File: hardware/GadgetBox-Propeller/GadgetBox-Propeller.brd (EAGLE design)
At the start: 93.5 x 53.5 mm, 13 parts, among them IC1 P8X32A-Q44

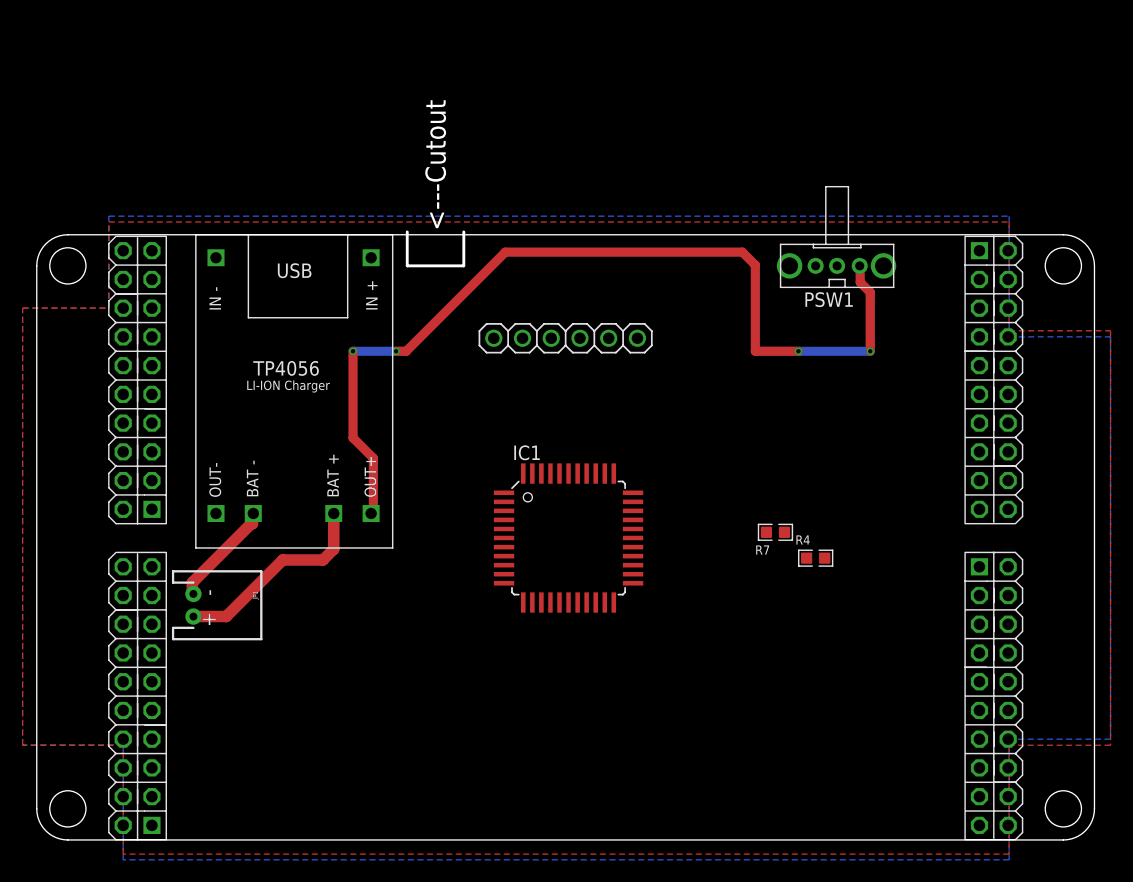
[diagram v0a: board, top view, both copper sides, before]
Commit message: mostly done routing
added EEPROM and most routing
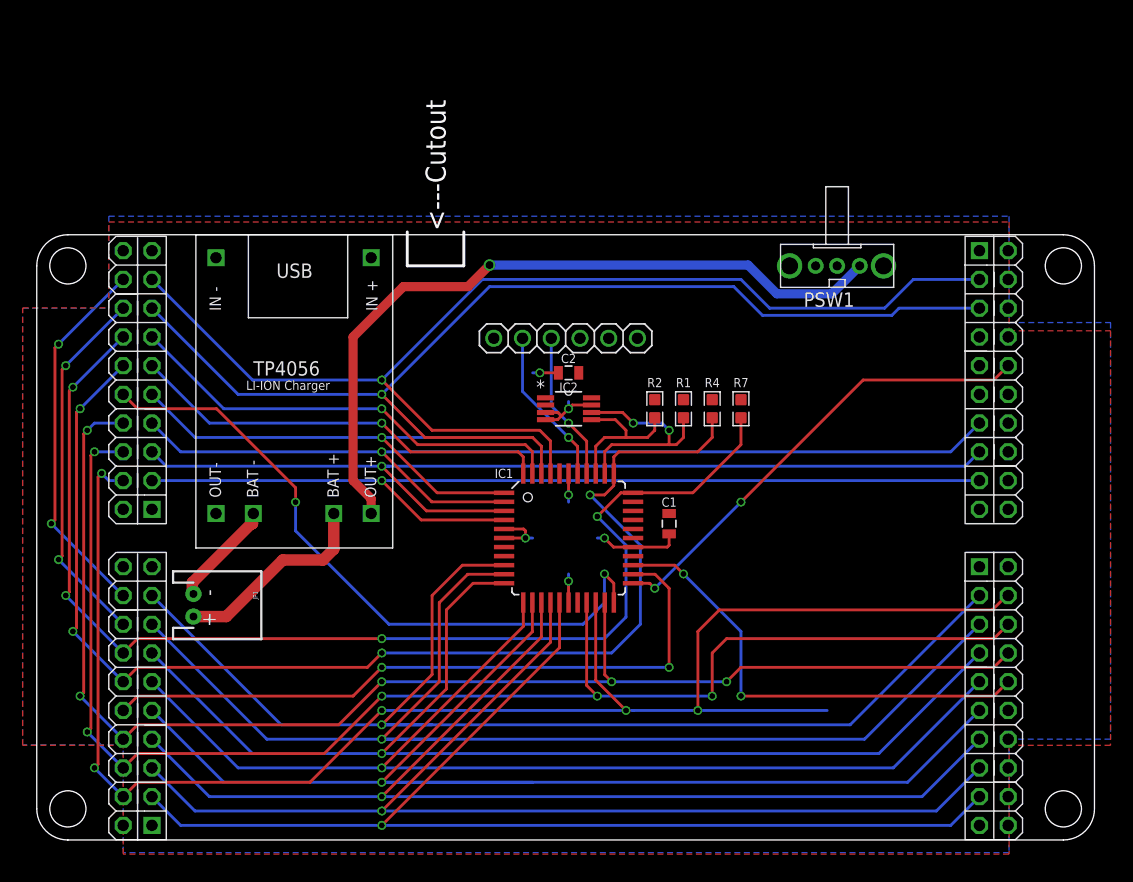
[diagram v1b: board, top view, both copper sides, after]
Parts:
- added C1, C2: (no value), SparkFun-Passives:0805
- added IC2: 24LC256-I/MS, Microchip_By_element14_Batch_1:SOP65P490X110-8N
- added R1, R2: 10K, GadgetFactory:0603
- moved R4 16.1 mm to (61.0, 39.4), turned to 90 degrees
- moved R7 11.3 mm to (63.5, 39.4), turned to 90 degrees
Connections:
- net 3V3: now also C1.1, C2.1, IC2.8, R1.2, R2.2
- net EEPROM-SCL: now also IC2.6, R1.1
- net EEPROM-SDA: now also IC2.5, R2.1
- net GND: now also C1.2, C2.2, IC2.3, IC2.4, IC2.7
- net IO0: now also AL.G0
- net IO1: now also AL.G1
- net IO2: now also AL.G2
- net IO3: now also AL.G3
- net IO4: now also AL.G4
- net IO5: now also AL.G5
- net IO6: now also AL.G6
- net IO7: now also AL.G7
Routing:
- net SPI-MISO: track 0.00 -> 143.8 mm, vias 0 -> 5
- net SPI-MOSI: track 0.00 -> 126.4 mm, vias 0 -> 5
- net SPI-SCK: track 0.00 -> 121.2 mm, vias 0 -> 5
- net IO12: track 0.00 -> 113.2 mm, vias 0 -> 1
- net IO9: track 0.00 -> 108.9 mm, vias 0 -> 1
- net I2C-SDA: track 0.00 -> 108.8 mm, vias 0 -> 4
- net IO8: track 0.00 -> 107.8 mm, vias 0 -> 1
- net I2C-SCL: track 0.00 -> 105.6 mm, vias 0 -> 4
- net IO0: track 0.00 -> 102.6 mm, vias 0 -> 1
- net IO10: track 0.00 -> 101.7 mm, vias 0 -> 1
- net IO15: track 0.00 -> 101.5 mm, vias 0 -> 1
- net IO14: track 0.00 -> 100.9 mm, vias 0 -> 1
- net IO13: track 0.00 -> 100.4 mm, vias 0 -> 1
- net IO1: track 0.00 -> 100.0 mm, vias 0 -> 1
- net IO11: track 0.00 -> 99.3 mm, vias 0 -> 1
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
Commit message: Propeller mostly done
Need to validate FTDI connection and do eCog graphics
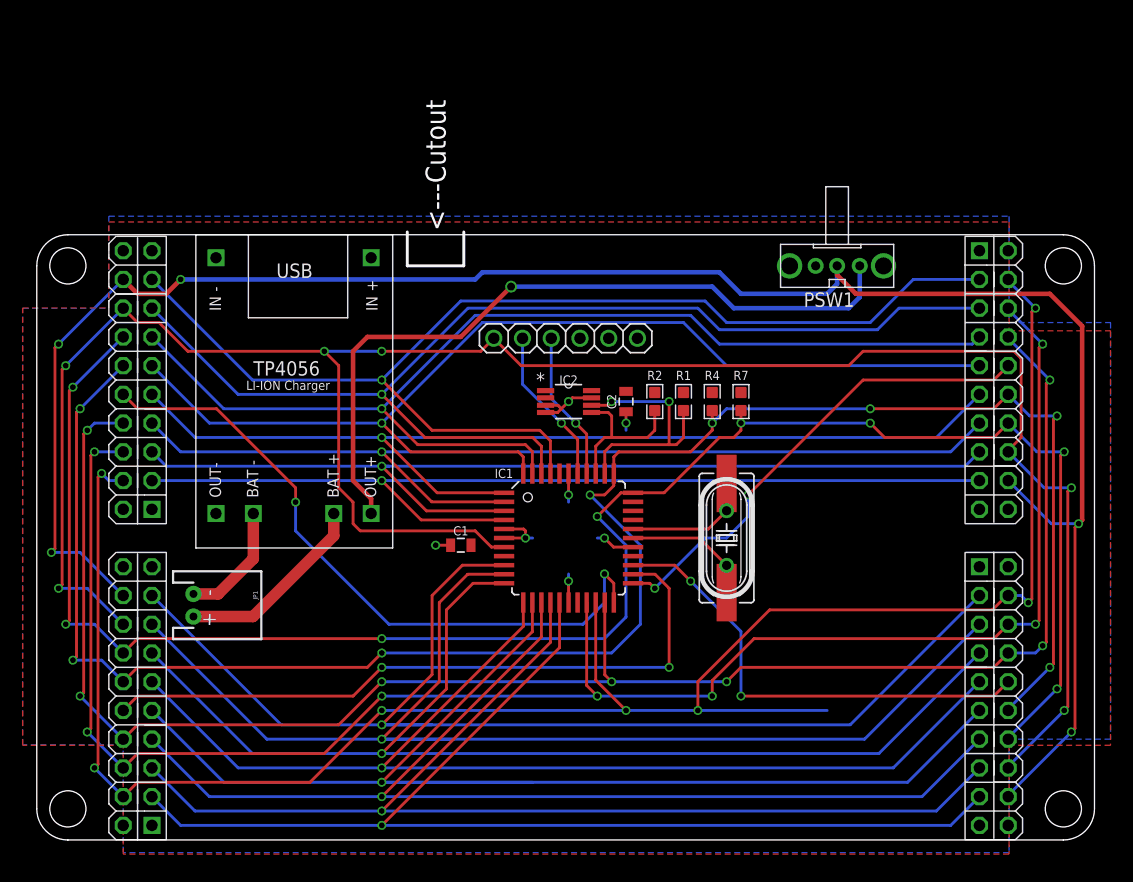
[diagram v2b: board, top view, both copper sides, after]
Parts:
- added Q1: (no value), adafruit:SM49
- added Q3: (no value), adafruit:HC49U-V
- moved C1 18.5 mm to (38.7, 27.3), turned to 180 degrees
- moved C2 5.68 mm to (53.3, 40.0), turned to 270 degrees
- moved IC2 0.64 mm to (48.3, 40.0)
- moved R1 0.64 mm to (58.4, 40.0)
- moved R2 0.64 mm to (55.9, 40.0)
- moved R4 0.64 mm to (61.0, 40.0)
- moved R7 0.64 mm to (63.5, 40.0)
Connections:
- removed net DTR: FTDI.1
- removed net N$1: IC1.7
- new net N$2: IC1.28, Q1.1, Q3.1
- new net N$3: IC1.29, Q1.2, Q3.2
- net RESET: now also FTDI.1, IC1.7
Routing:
- net RESET: track 32.7 -> 190.6 mm, vias 2 -> 6
- net VIN: track 33.2 -> 178.3 mm, vias 2 -> 5
- net I2C-SDA: track 108.8 -> 170.7 mm, vias 4 -> 8
- net I2C-SCL: track 105.6 -> 165.1 mm, vias 4 -> 8
- net IO3: track 37.6 -> 95.7 mm
- net IO2: track 39.8 -> 97.3 mm
- net IO4: track 48.1 -> 89.1 mm
- net SPI-SCK: track 121.2 -> 153.6 mm, vias 5 -> 7
- net SPI-MOSI: track 126.4 -> 156.9 mm, vias 5 -> 7
- net SPI-MISO: track 143.8 -> 173.1 mm, vias 5 -> 7
- net N$2: track 0.00 -> 11.7 mm
- net N$3: track 0.00 -> 11.6 mm
- net GND: track 36.4 -> 33.6 mm, vias 6 -> 7
- net EEPROM-SCL: track 19.9 -> 22.6 mm
- net SPI-CSB: track 41.5 -> 42.6 mm
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
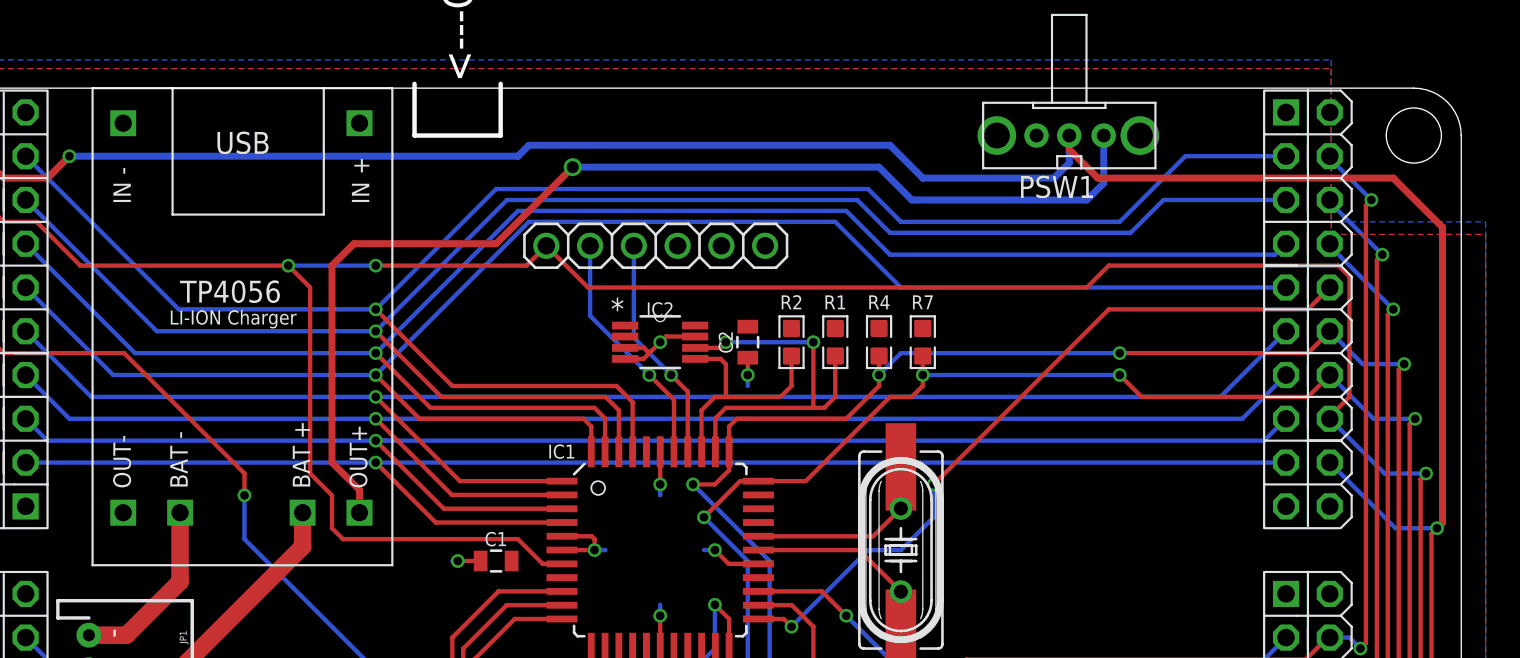
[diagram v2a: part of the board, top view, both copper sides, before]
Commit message: Increased the size of the pads on the battery charge unit to allow surface mount soldering.
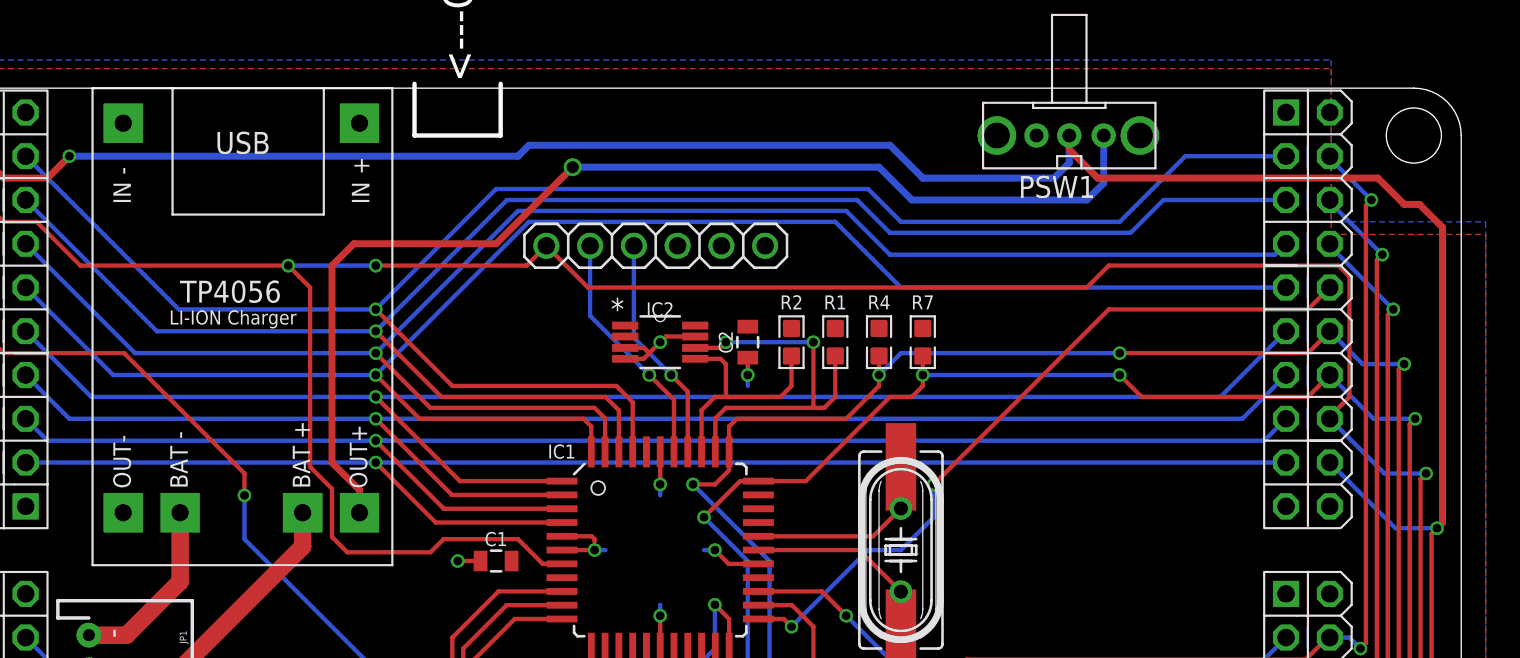
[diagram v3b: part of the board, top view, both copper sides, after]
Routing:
- net RESET: track 190.6 -> 191.5 mm
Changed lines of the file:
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@@
 <setting verticaltext="up"/>
 </settings>
-<grid distance="0.0125" unitdist="inch" unit="inch" style="lines" multiple="1" display="yes" altdistance="0.005" altunitdist="inch" altunit="inch"/>
+<grid distance="0.05" unitdist="inch" unit="inch" style="lines" multiple="1" display="yes" altdistance="0.005" altunitdist="inch" altunit="inch"/>
 <layers>
 <layer number="1" name="Top" color="4" fill="1" visible="yes" active="yes"/>
@@
 <wire x1="42.56" y1="27.14" x2="41.44" y2="27.14" width="0.254" layer="1"/>
 <wire x1="41.44" y1="27.14" x2="40.005" y2="28.575" width="0.254" layer="1"/>
-<wire x1="40.005" y1="28.575" x2="29.845" y2="28.575" width="0.254" layer="1"/>
-<wire x1="29.845" y1="28.575" x2="29.21" y2="29.21" width="0.254" layer="1"/>
-<wire x1="29.21" y1="29.21" x2="29.21" y2="31.115" width="0.254" layer="1"/>
-<wire x1="29.21" y1="31.115" x2="27.94" y2="32.385" width="0.254" layer="1"/>
-<wire x1="27.94" y1="32.385" x2="27.94" y2="43.18" width="0.254" layer="1"/>
+<wire x1="27.94" y1="34.925" x2="27.94" y2="35.433" width="0.254" layer="1"/>
+<wire x1="27.94" y1="35.433" x2="27.94" y2="43.18" width="0.254" layer="1"/>
 <wire x1="27.94" y1="43.18" x2="26.67" y2="44.45" width="0.254" layer="1"/>
 <via x="26.67" y="44.45" extent="1-16" drill="0.5"/>
@@
 <wire x1="73.025" y1="43.18" x2="44.07" y2="43.18" width="0.254" layer="1"/>
 <wire x1="44.07" y1="43.18" x2="41.65" y2="45.6" width="0.254" layer="1"/>
+<wire x1="40.005" y1="28.575" x2="35.687" y2="28.575" width="0.254" layer="1"/>
+<wire x1="35.687" y1="28.575" x2="34.925" y2="27.813" width="0.254" layer="1"/>
+<wire x1="34.925" y1="27.813" x2="30.099" y2="27.813" width="0.254" layer="1"/>
+<wire x1="30.099" y1="27.813" x2="29.21" y2="28.702" width="0.254" layer="1"/>
+<wire x1="29.21" y1="28.702" x2="29.21" y2="31.496" width="0.254" layer="1"/>
+<wire x1="29.21" y1="31.496" x2="27.94" y2="32.766" width="0.254" layer="1"/>
+<wire x1="27.94" y1="32.766" x2="27.94" y2="34.925" width="0.254" layer="1"/>
 </signal>
 <signal name="SPI-SCK">
@@
 <wire x1="72" y1="52" x2="72" y2="51.19" width="0.4064" layer="1"/>
 <wire x1="72" y1="51.19" x2="73.66" y2="49.53" width="0.4064" layer="1"/>
-<wire x1="73.66" y1="49.53" x2="90.805" y2="49.53" width="0.4064" layer="1"/>
-<wire x1="90.805" y1="49.53" x2="93.6625" y2="46.6725" width="0.4064" layer="1"/>
 <wire x1="93.6625" y1="46.6725" x2="93.6625" y2="29.5275" width="0.4064" layer="1"/>
 <wire x1="93.6625" y1="29.5275" x2="93.345" y2="29.21" width="0.4064" layer="1"/>
@@
 <wire x1="12.7" y1="49.53" x2="10.16" y2="49.53" width="0.4064" layer="1"/>
 <wire x1="10.16" y1="49.53" x2="8.89" y2="50.8" width="0.4064" layer="1"/>
+<wire x1="73.66" y1="49.53" x2="89.916" y2="49.53" width="0.4064" layer="1"/>
+<wire x1="89.916" y1="49.53" x2="91.44" y2="48.006" width="0.4064" layer="1"/>
+<wire x1="91.44" y1="48.006" x2="92.329" y2="48.006" width="0.4064" layer="1"/>
+<wire x1="92.329" y1="48.006" x2="93.6625" y2="46.6725" width="0.4064" layer="1"/>
 </signal>
 <signal name="VOUT">
@@
 </signal>
 </signals>
+<errors>
+</errors>
 </board>
 </drawing>
